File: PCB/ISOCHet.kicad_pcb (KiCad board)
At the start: 2 copper layers, 57.1 x 38.1 mm, 19 parts, among them J1 USB_C_Receptacle_USB2.0, J2 Conn_01x08_Pin, SW0 BOOT, SW1 TAB, SW2 ENTER, SW3 CAPS, SW4 CAPS_STEP1.5, SW5 CAPS_STEP1.25, U1 CH552G, U2 USBLC6-2P6

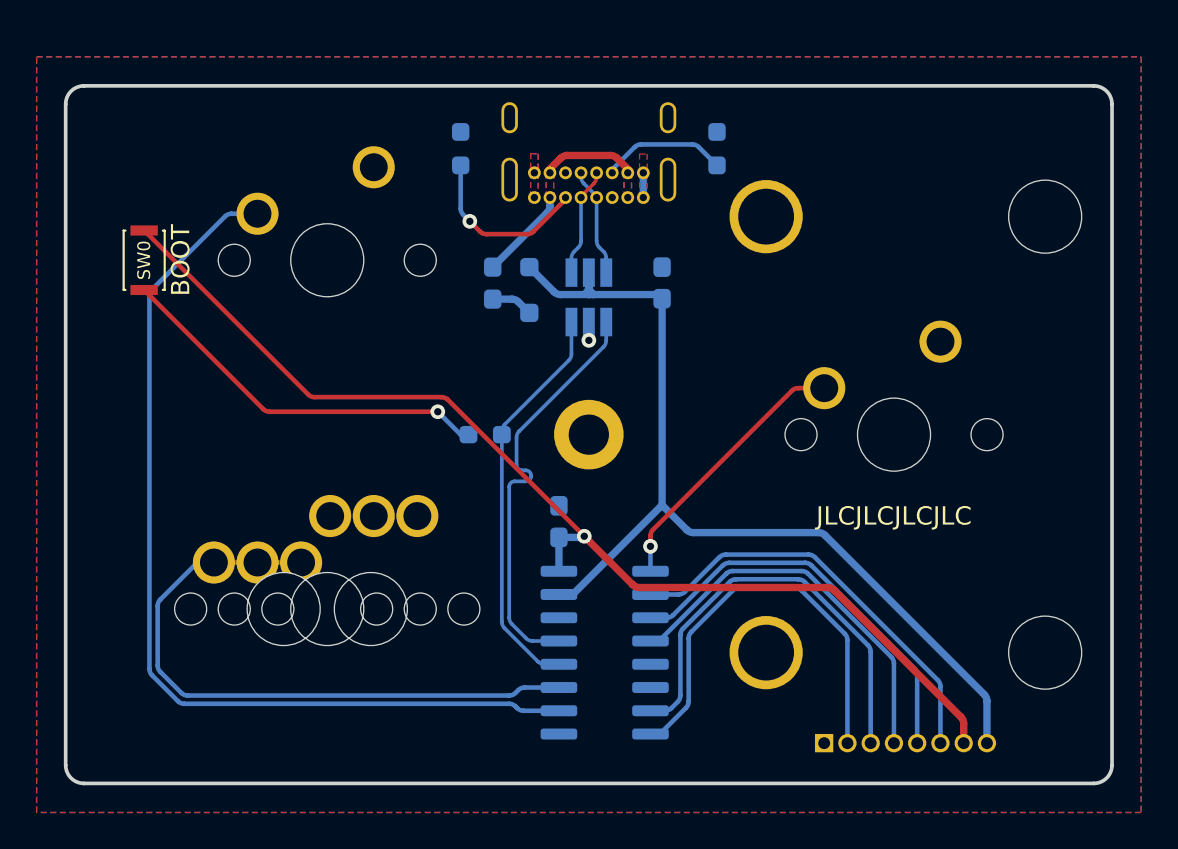
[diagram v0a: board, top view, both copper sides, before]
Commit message: Flip USB port to top side; add 3D models
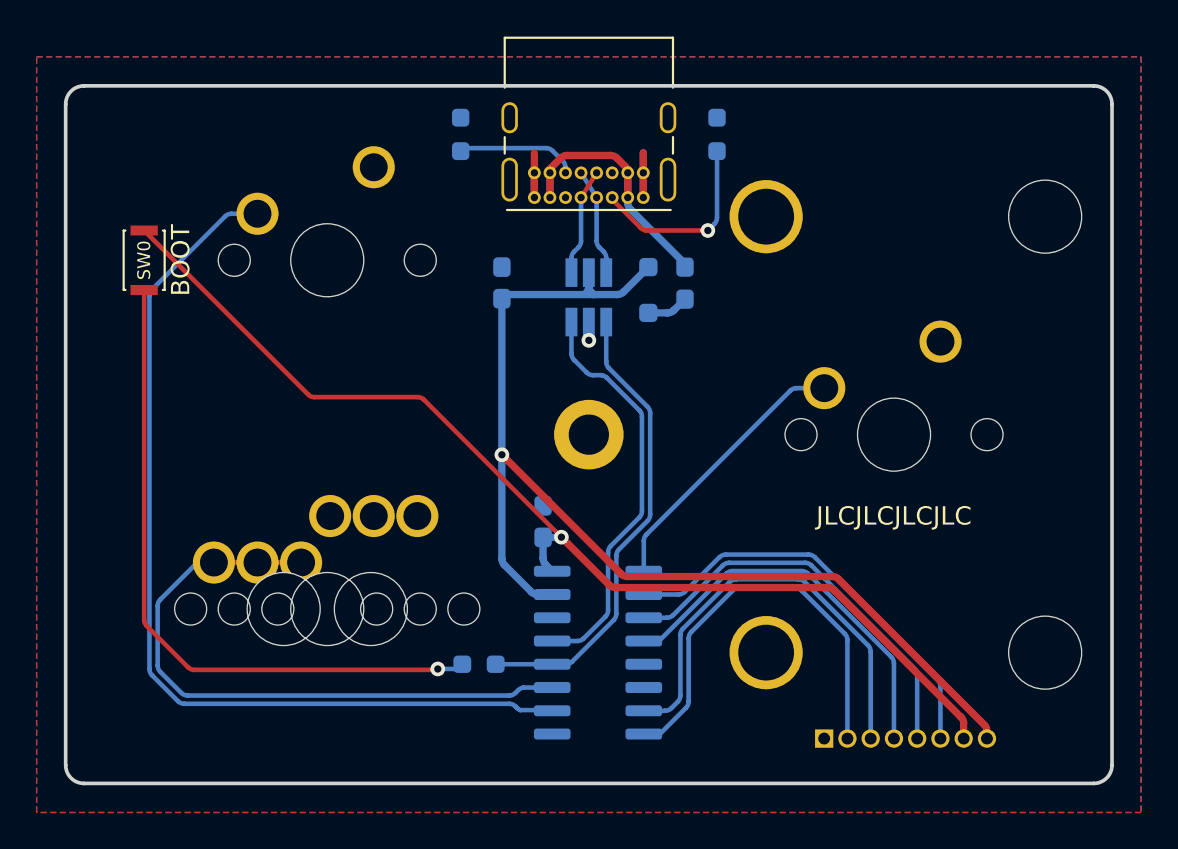
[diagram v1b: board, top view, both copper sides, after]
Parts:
- J1: moved to F.Cu
- moved R3 12.5 mm to (152.8, 69.7)
- moved F1 10.5 mm to (164.0, 48.9)
- moved C1 8.75 mm to (154.0, 48.9)
- moved D1 6.50 mm to (162.0, 49.2)
- moved J1 5.95 mm to (161.7, 44.2), turned to 180 degrees
- moved C2 0.87 mm to (156.2, 61.9)
- moved R1 0.78 mm to (165.8, 40.8)
- moved R2 0.78 mm to (151.8, 40.8)
- moved U1 0.37 mm to (159.2, 69.1)
- moved J2 0.25 mm to (171.6, 73.8)
- renumbered R2 to R1, R1 to R2
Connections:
- J1 pad A6: P_D+ -> P_DP
- J1 pad A7: P_D- -> P_DM
- J1 pad B6: P_D+ -> P_DP
- J1 pad B7: P_D- -> P_DM
- R1 pad 1: Net-(J1-CC2) -> Net-(J1-CC1)
- R2 pad 1: Net-(J1-CC1) -> Net-(J1-CC2)
- R3 pad 1: D+ -> UDP
- U1 pad 12: D+ -> UDP
- U1 pad 13: D- -> UDM
- U2 pad 1: D- -> UDP
- U2 pad 3: D+ -> UDM
- U2 pad 4: P_D+ -> P_DM
- U2 pad 6: P_D- -> P_DP
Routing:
- net UDP: track 0.00 -> 24.6 mm
- net UDM: track 0.00 -> 22.3 mm
- net D-: track 22.0 -> 0.00 mm
- net D+: track 21.3 -> 0.00 mm
- net Net-(R3-Pad2): track 21.0 -> 36.4 mm
- net VCC: track 52.8 -> 61.0 mm, vias 0 -> 1
- net GND: track 1.35 -> 8.68 mm
- net P_DP: track 0.00 -> 5.86 mm
- net P_DM: track 0.00 -> 5.86 mm
- net P_D-: track 5.65 -> 0.00 mm
- net P_D+: track 5.65 -> 0.00 mm
- net VBUS: track 10.3 -> 15.5 mm
- net Net-(J1-CC1): track 9.49 -> 10.4 mm
- net Net-(J2-Pin_3): track 23.0 -> 23.9 mm
- net Net-(J2-Pin_2): track 22.6 -> 23.3 mm
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- removed copper zone on B.Cu, net VBUS
- removed copper zone on F.Cu, net VBUS

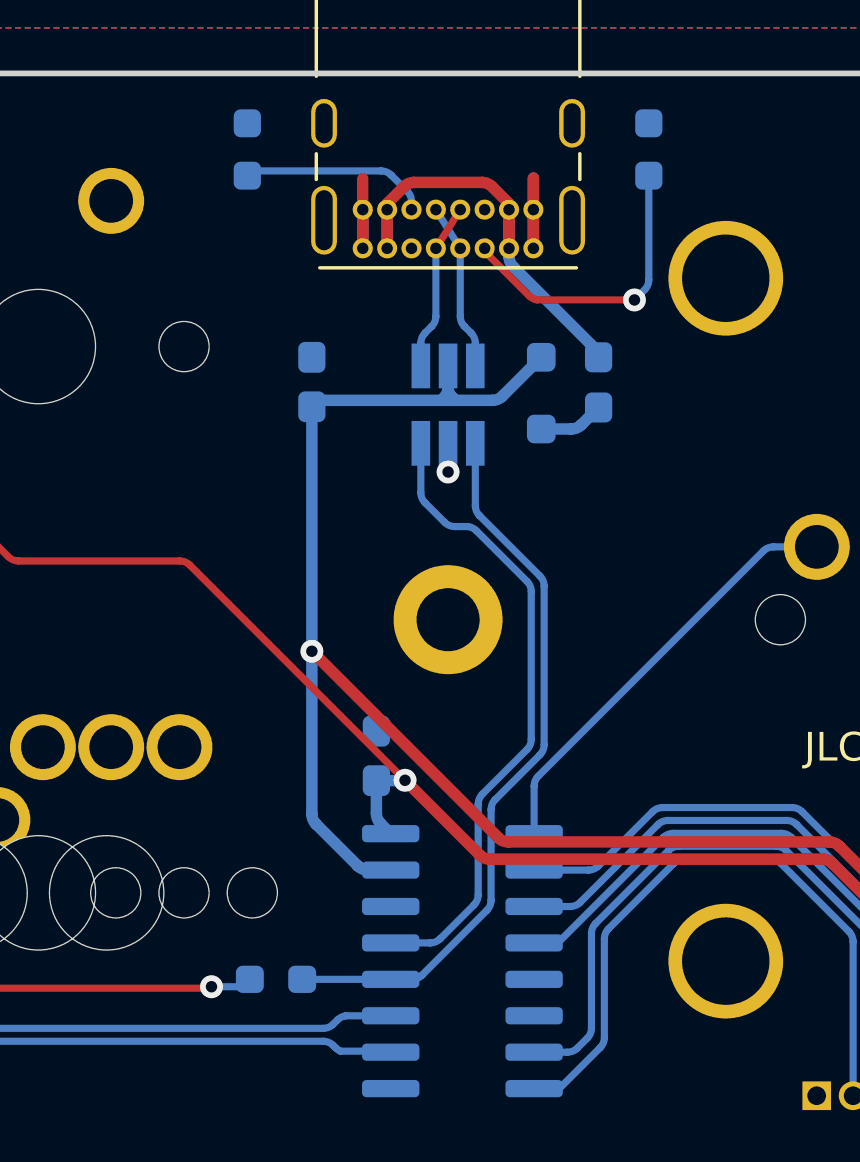
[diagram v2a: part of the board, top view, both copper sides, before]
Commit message: Move OSHW logo to front, PCB name, etc. to back, and straighten a few traces
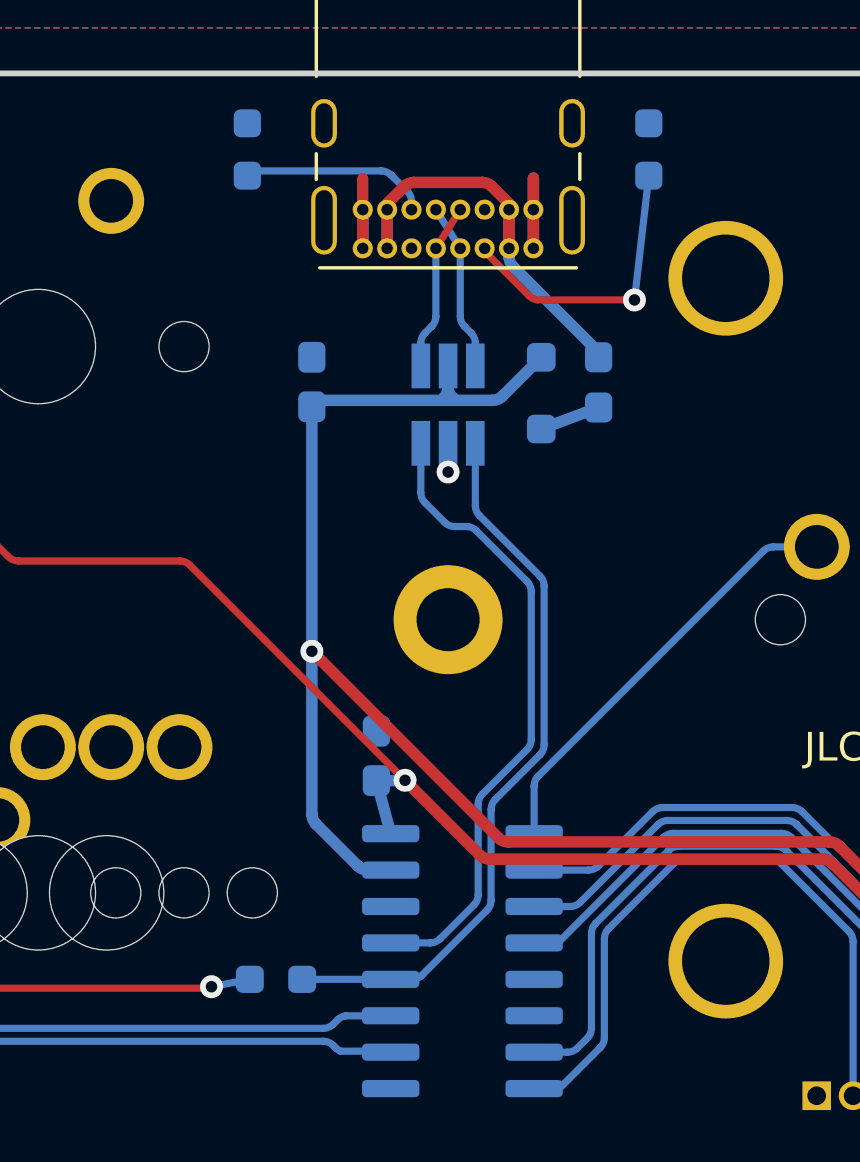
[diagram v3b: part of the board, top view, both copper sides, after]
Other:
- board text added: "ISOCHet"
- board text added: "v1.0 by bgkendall"
- board text removed: "ISOCHet v1.0"
- board text removed: "bgkendall"

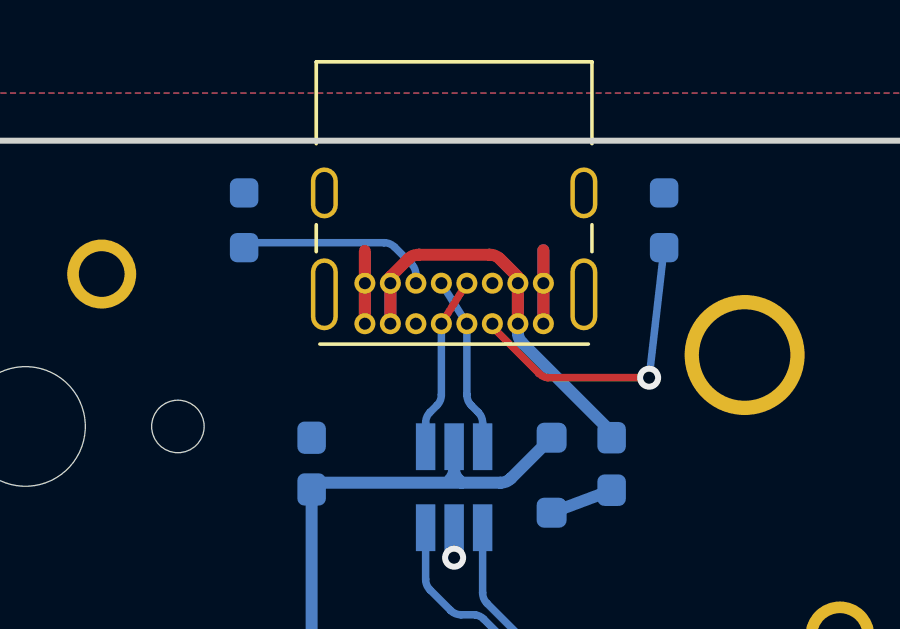
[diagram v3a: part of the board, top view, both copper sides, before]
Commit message: Swap R1 and R2
There’s more room for the via on the other side of the USB port.
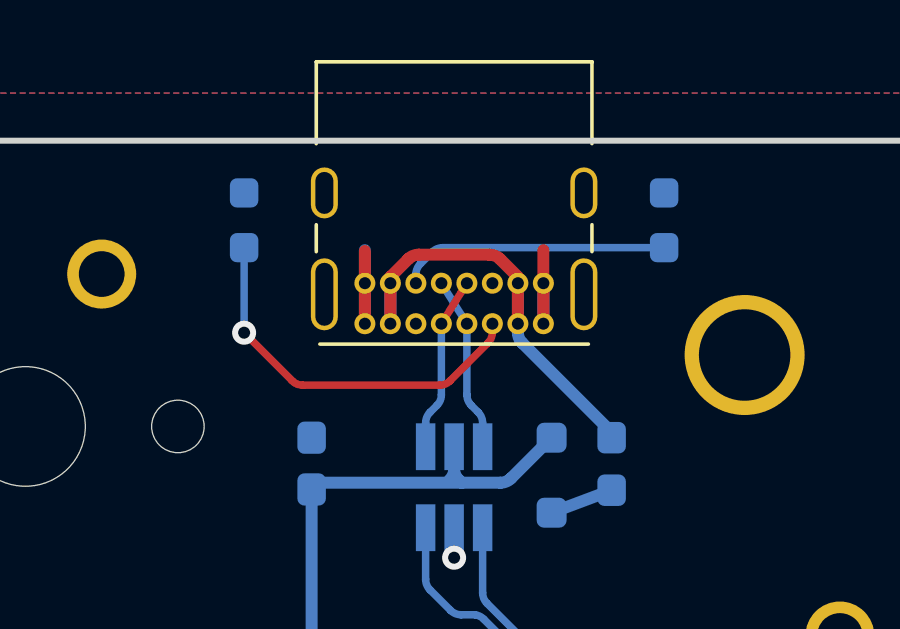
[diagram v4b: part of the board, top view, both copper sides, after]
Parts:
- renumbered R2 to R1, R1 to R2
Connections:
- R1 pad 1: Net-(J1-CC2) -> Net-(J1-CC1)
- R2 pad 1: Net-(J1-CC1) -> Net-(J1-CC2)
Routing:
- net Net-(J1-CC2): track 6.36 -> 9.01 mm
- net Net-(J1-CC1): track 10.3 -> 12.9 mm
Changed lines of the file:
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@@
     (descr "https://www.ckswitches.com/media/1465/kxt3.pdf")
     (tags "Switch SPST KXT3")
+    (property "LSCC" "C221821")
     (property "Sheetfile" "ISOCHet.kicad_sch")
     (property "Sheetname" "")
@@
     (property "ki_keywords" "R res resistor")
     (attr smd)
-    (fp_text reference "R1" (at 0 1.43 90) (layer "B.SilkS")
+    (fp_text reference "R2" (at 0 1.43 90) (layer "B.SilkS")
         (effects (font (size 1 1) (thickness 0.15)) (justify mirror))
     )
@@
       (stroke (width 0.1) (type solid)) (layer "B.Fab"))
     (pad "1" smd roundrect (at -0.9125 0 90) (size 0.975 0.95) (layers "B.Cu" "B.Paste" "B.Mask") (roundrect_rratio 0.25)
-      (net 5 "Net-(J1-CC1)") (pintype "passive"))
+      (net 9 "Net-(J1-CC2)") (pintype "passive"))
     (pad "2" smd roundrect (at 0.9125 0 90) (size 0.975 0.95) (layers "B.Cu" "B.Paste" "B.Mask") (roundrect_rratio 0.25)
       (net 2 "GND") (pintype "passive"))
@@
     (descr "Capacitor SMD 0603 (1608 Metric), square (rectangular) end terminal, IPC_7351 nominal with elongated pad for handsoldering. (Body size source: IPC-SM-782 page 76, https://www.pcb-3d.com/wordpress/wp-content/uploads/ipc-sm-782a_amendment_1_and_2.pdf), generated with kicad-footprint-generator")
     (tags "capacitor handsolder")
-    (property "LSCC" "C1525 ")
+    (property "LSCC" "C1525")
     (property "Sheetfile" "ISOCHet.kicad_sch")
     (property "Sheetname" "")
@@
     (property "ki_keywords" "R res resistor")
     (attr smd)
-    (fp_text reference "R2" (at 0 -1.36 90) (layer "B.SilkS")
+    (fp_text reference "R1" (at 0 -1.36 90) (layer "B.SilkS")
         (effects (font (size 1 1) (thickness 0.15)) (justify mirror))
     )
@@
       (stroke (width 0.1) (type solid)) (layer "B.Fab"))
     (pad "1" smd roundrect (at -0.9125 0 90) (size 0.975 0.95) (layers "B.Cu" "B.Paste" "B.Mask") (roundrect_rratio 0.25)
-      (net 9 "Net-(J1-CC2)") (pintype "passive"))
+      (net 5 "Net-(J1-CC1)") (pintype "passive"))
     (pad "2" smd roundrect (at 0.9125 0 90) (size 0.975 0.95) (layers "B.Cu" "B.Paste" "B.Mask") (roundrect_rratio 0.25)
       (net 2 "GND") (pintype "passive"))
@@
   (segment (start 161.725 42.85) (end 161.725 44.2) (width 0.4) (layer "F.Cu") (net 2))
   (via (at 158.75 52) (size 0.8) (drill 0.4) (layers "F.Cu" "B.Cu") (free) (net 2))
-  (segment (start 161.725 44.2) (end 161.725 41.75) (width 0.4) (layer "B.Cu") (net 2))
-  (segment (start 155.775 44.2) (end 155.775 42.85) (width 0.4) (layer "B.Cu") (net 2))
+  (segment (start 161.725 44.2) (end 161.725 42.85) (width 0.4) (layer "B.Cu") (net 2))
+  (segment (start 155.775 44.2) (end 155.775 41.75) (width 0.4) (layer "B.Cu") (net 2))
   (segment (start 162 50.5) (end 164 49.75) (width 0.4) (layer "B.Cu") (net 3))
   (segment (start 159.928554 41.9) (end 157.571446 41.9) (width 0.4) (layer "F.Cu") (net 4))
@@
   (segment (start 160.875 44.2) (end 160.875 44.487867) (width 0.4) (layer "B.Cu") (net 4))
   (arc (start 161.021447 44.841421) (mid 160.91306 44.679209) (end 160.875 44.487867) (width 0.4) (layer "B.Cu") (net 4))
-  (segment (start 165.248054 45.998054) (end 161.861941 45.998054) (width 0.25) (layer "F.Cu") (net 5))
-  (segment (start 161.573958 45.853553) (end 160.025 44.304595) (width 0.25) (layer "F.Cu") (net 5))
-  (segment (start 165.25 46) (end 165.248054 45.998054) (width 0.25) (layer "F.Cu") (net 5))
-  (via (at 165.25 46) (size 0.8) (drill 0.4) (layers "F.Cu" "B.Cu") (net 5))
-  (arc (start 161.861941 45.998054) (mid 161.706368 45.948433) (end 161.573958 45.853553) (width 0.25) (layer "F.Cu") (net 5))
-  (segment (start 165.25 46) (end 165.75 41.665) (width 0.25) (layer "B.Cu") (net 5))
+  (segment (start 160.025 44.487867) (end 160.025 44.2) (width 0.25) (layer "F.Cu") (net 5))
+  (segment (start 151.75 44.5) (end 153.353554 46.103554) (width 0.25) (layer "F.Cu") (net 5))
+  (segment (start 158.616421 46.103553) (end 159.878554 44.84142) (width 0.25) (layer "F.Cu") (net 5))
+  (segment (start 153.707107 46.25) (end 158.262867 46.25) (width 0.25) (layer "F.Cu") (net 5))
+  (via (at 151.75 44.5) (size 0.8) (drill 0.4) (layers "F.Cu" "B.Cu") (net 5))
+  (arc (start 158.262867 46.25) (mid 158.454209 46.21194) (end 158.616421 46.103553) (width 0.25) (layer "F.Cu") (net 5))
+  (arc (start 160.025 44.487867) (mid 159.98694 44.679208) (end 159.878554 44.84142) (width 0.25) (layer "F.Cu") (net 5))
+  (arc (start 153.353554 46.103554) (mid 153.515766 46.21194) (end 153.707107 46.25) (width 0.25) (layer "F.Cu") (net 5))
+  (segment (start 151.75 44.5) (end 151.75 41.665) (width 0.25) (layer "B.Cu") (net 5))
   (segment (start 159.175 44.2) (end 159.175 46.567893) (width 0.25) (layer "B.Cu") (net 6))
   (segment (start 159.7 47.507107) (end 159.7 48.3) (width 0.25) (layer "B.Cu") (net 6))
@@
   (arc (start 157.8 47.507107) (mid 157.83806 47.315766) (end 157.946446 47.153554) (width 0.25) (layer "B.Cu") (net 7))
   (arc (start 158.325 46.567893) (mid 158.28694 46.759235) (end 158.178553 46.921447) (width 0.25) (layer "B.Cu") (net 7))
-  (segment (start 151.915 41.5) (end 156.412867 41.5) (width 0.25) (layer "B.Cu") (net 9))
-  (segment (start 156.766421 41.646447) (end 157.328554 42.20858) (width 0.25) (layer "B.Cu") (net 9))
-  (segment (start 157.475 42.562133) (end 157.475 42.85) (width 0.25) (layer "B.Cu") (net 9))
-  (arc (start 157.328554 42.20858) (mid 157.43694 42.370792) (end 157.475 42.562133) (width 0.25) (layer "B.Cu") (net 9))
-  (arc (start 156.412867 41.5) (mid 156.604207 41.538071) (end 156.766421 41.646447) (width 0.25) (layer "B.Cu") (net 9))
+  (segment (start 157.621447 42.208579) (end 158.01858 41.811446) (width 0.25) (layer "B.Cu") (net 9))
+  (segment (start 158.372133 41.665) (end 165.75 41.665) (width 0.25) (layer "B.Cu") (net 9))
+  (segment (start 157.475 42.85) (end 157.475 42.562133) (width 0.25) (layer "B.Cu") (net 9))
+  (arc (start 158.372133 41.665) (mid 158.180792 41.70306) (end 158.01858 41.811446) (width 0.25) (layer "B.Cu") (net 9))
+  (arc (start 157.621447 42.208579) (mid 157.51306 42.370791) (end 157.475 42.562133) (width 0.25) (layer "B.Cu") (net 9))
   (segment (start 159.7 51) (end 159.7 53.167157) (width 0.25) (layer "B.Cu") (net 11))
   (segment (start 160.25 63.772793) (end 160.25 66.929289) (width 0.25) (layer "B.Cu") (net 11))
